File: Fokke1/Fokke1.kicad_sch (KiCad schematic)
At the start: 95 parts, among them J1 Conn_02x20_Top_Bottom, SW1 SW_SPST, SW10 SW_SPST, SW11 SW_SPST, SW12 SW_SPST, SW2 SW_SPST, SW3 SW_SPST, SW4 SW_SPST, SW5 SW_SPST, SW6 SW_SPST, SW7 SW_SPST, SW8 SW_SPST, SW9 SW_SPST

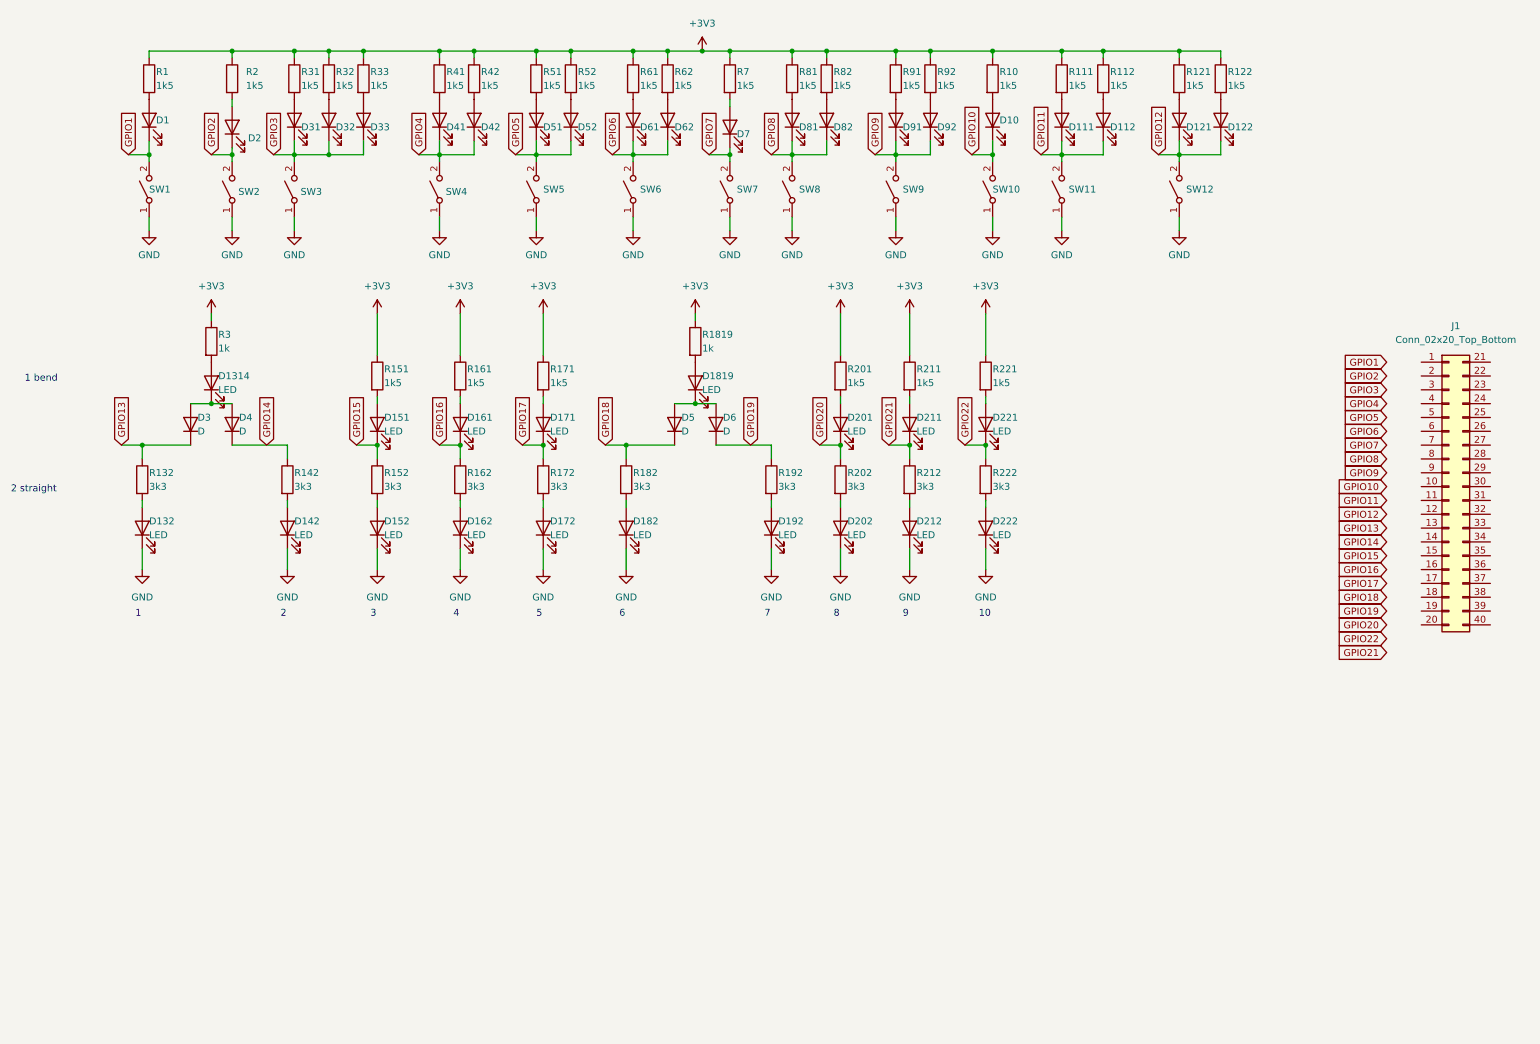
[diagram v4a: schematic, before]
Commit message: I added a button to Fokke 1 for his gate, but I lost annonation with the schematic. The schematic as is now is FUBAR. The project however is finished so I got lucky...
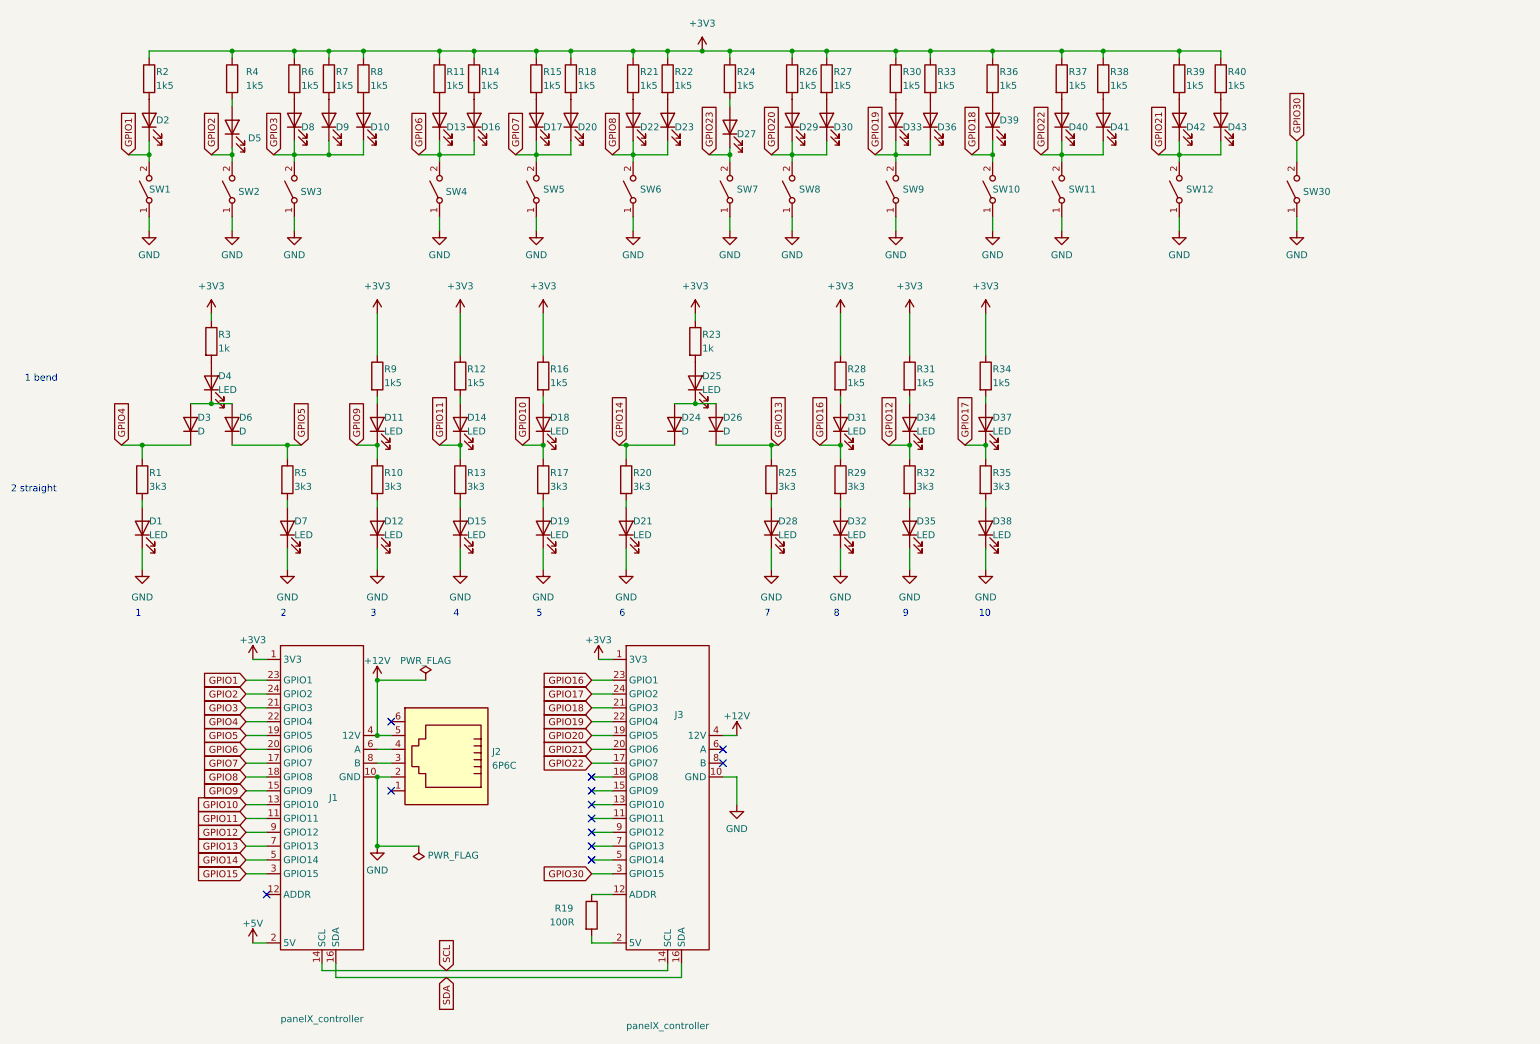
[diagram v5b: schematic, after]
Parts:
- removed J1: Conn_02x20_Top_Bottom, Connector_PinHeader_2.54mm:PinHeader_2x20_P2.54mm_Vertical_SMD, symbol Connector_Generic:Conn_02x20_Top_Bottom
- added J1, J3: panelX_controller, custom_kicad_lib_sk:panelX_contoller, symbol custom_kicad_lib_sk:panelX_controller
- added J2: 6P6C, Connector_RJ:RJ12_Amphenol_54601, symbol Connector:6P6C
- added R19: 100R, Resistor_SMD:R_0805_2012Metric_Pad1.20x1.40mm_HandSolder, symbol Device:R
- added SW30: SW_SPST, custom_kicad_lib_sk:SW_NO_SILK, symbol Switch:SW_SPST
- renumbered D132 to D1, D33 to D10, D151 to D11, D152 to D12, D41 to D13, D161 to D14, D162 to D15, D42 to D16, D51 to D17, D171 to D18, D172 to D19, D1 to D2, D52 to D20, D182 to D21, D61 to D22, D62 to D23, D5 to D24, D1819 to D25, D6 to D26, D7 to D27, D192 to D28, D81 to D29, D82 to D30, D201 to D31, D202 to D32, D91 to D33, D211 to D34, D212 to D35, D92 to D36, D221 to D37, D222 to D38, D10 to D39, D1314 to D4, D111 to D40, D112 to D41, D121 to D42, D122 to D43, D2 to D5, D4 to D6, D142 to D7, D31 to D8, D32 to D9, R132 to R1, R152 to R10, R41 to R11, R161 to R12, R162 to R13, R42 to R14, R51 to R15, R171 to R16, R172 to R17, R52 to R18, R1 to R2, R182 to R20, R61 to R21, R62 to R22, R1819 to R23, R7 to R24, R192 to R25, R81 to R26, R82 to R27, R201 to R28, R202 to R29, R91 to R30, R211 to R31, R212 to R32, R92 to R33, R221 to R34, R222 to R35, R10 to R36, R111 to R37, R112 to R38, R121 to R39, R2 to R4, R122 to R40, R142 to R5, R31 to R6, R32 to R7, R33 to R8, R151 to R9
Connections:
- net +3V3: now also J1.1 (3V3), J3.1 (3V3)
- net GND: now also J1.10 (GND), J2.2, J3.10 (GND), SW30.1 (A)
- net GPIO1: now also J1.23 (GPIO1)
- net GPIO10: now also D18.1 (K), R17.1, J1.13 (GPIO10); no longer D39.1 (K), SW10.2 (B)
- net GPIO11: now also D14.1 (K), R13.1, J1.11 (GPIO11); no longer D40.1 (K), D41.1 (K), SW11.2 (B)
- net GPIO12: now also D34.1 (K), R32.1, J1.9 (GPIO12); no longer D42.1 (K), D43.1 (K), SW12.2 (B)
- net GPIO13: now also D26.1 (K), R25.1, J1.7 (GPIO13); no longer D3.1 (K), R1.1
- net GPIO14: now also D24.1 (K), R20.1, J1.5 (GPIO14); no longer D6.1 (K), R5.1
- net GPIO15: now also J1.3 (GPIO15); no longer D11.1 (K), R10.1
- net GPIO16: now also D31.1 (K), R29.1, J3.23 (GPIO1); no longer D14.1 (K), R13.1
- net GPIO17: now also D37.1 (K), R35.1, J3.24 (GPIO2); no longer D18.1 (K), R17.1
- net GPIO18: now also D39.1 (K), SW10.2 (B), J3.21 (GPIO3); no longer D24.1 (K), R20.1
- net GPIO19: now also D33.1 (K), D36.1 (K), SW9.2 (B), J3.22 (GPIO4); no longer D26.1 (K), R25.1
- net GPIO2: now also J1.24 (GPIO2)
- net GPIO20: now also D29.1 (K), D30.1 (K), SW8.2 (B), J3.19 (GPIO5); no longer D31.1 (K), R29.1
- net GPIO21: now also D42.1 (K), D43.1 (K), SW12.2 (B), J3.20 (GPIO6); no longer D34.1 (K), R32.1
- net GPIO22: now also D40.1 (K), D41.1 (K), SW11.2 (B), J3.17 (GPIO7); no longer D37.1 (K), R35.1
- net GPIO3: now also J1.21 (GPIO3)
- net GPIO4: now also D3.1 (K), R1.1, J1.22 (GPIO4); no longer D13.1 (K), D16.1 (K), SW4.2 (B)
- net GPIO5: now also D6.1 (K), R5.1, J1.19 (GPIO5); no longer D17.1 (K), D20.1 (K), SW5.2 (B)
- net GPIO6: now also D13.1 (K), D16.1 (K), SW4.2 (B), J1.20 (GPIO6); no longer D22.1 (K), D23.1 (K), SW6.2 (B)
- net GPIO7: now also D17.1 (K), D20.1 (K), SW5.2 (B), J1.17 (GPIO7); no longer D27.1 (K), SW7.2 (B)
- net GPIO8: now also D22.1 (K), D23.1 (K), SW6.2 (B), J1.18 (GPIO8); no longer D29.1 (K), D30.1 (K), SW8.2 (B)
- net GPIO9: now also D11.1 (K), R10.1, J1.15 (GPIO9); no longer D33.1 (K), D36.1 (K), SW9.2 (B)
- new net: J3.12 (ADDR), R19.1
- new net: J3.2 (5V), R19.2
- new net: J1.6 (A), J2.4
- new net: J1.8 (B), J2.3
- new net +12V: J1.4 (12V), J2.5, J3.4 (12V)
- new net +5V: J1.2 (5V)
- new net GPIO23: D27.1 (K), SW7.2 (B)
- new net GPIO30: J3.3 (GPIO15), SW30.2 (B)
- new net SCL: J1.14 (SCL), J3.14 (SCL)
- new net SDA: J1.16 (SDA), J3.16 (SDA)
- no-connect marks 0 -> 12
